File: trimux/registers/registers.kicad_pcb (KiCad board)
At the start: 2 copper layers, 69 parts, among them P1 CONN_02X05, P2 CONN_02X08, P3 CONN_01X04, P4 CONN_01X02, P5 CONN_01X02, P6 CONN_01X02, P7 CONN_01X02, P8 CONN_01X02, P9 CONN_01X02, U1 trimux, U10 trimux, U12 trimux, U2 trimux, U3 trimux, U4 trimux, U5 trimux, U6 trimux, U7 LM324, U8 trimux, U9 trimux

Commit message: registers
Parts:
- added C1: 47u, Capacitors_THT:CP_Radial_D5.0mm_P2.50mm, F.Cu at (91.1, 57.1)
- added C10: 47u, Capacitors_THT:CP_Radial_D5.0mm_P2.50mm, F.Cu at (77.3, 109.2)
- added C11: 47u, Capacitors_THT:CP_Radial_D5.0mm_P2.50mm, F.Cu at (95.1, 106.7)
- added C12: 104, Capacitors_SMD:C_1206_HandSoldering, B.Cu at (66.5, 22.2)
- added C13: 104, Capacitors_SMD:C_1206_HandSoldering, B.Cu at (88.7, 26.0)
- added C14: 104, Capacitors_SMD:C_1206_HandSoldering, B.Cu at (105.2, 24.1)
- added C2: 47u, Capacitors_THT:CP_Radial_D5.0mm_P2.50mm, F.Cu at (74.1, 57.1)
- added C3: 104, Capacitors_SMD:C_1206_HandSoldering, B.Cu at (99.5, 51.4)
- added C4: 104, Capacitors_SMD:C_1206_HandSoldering, B.Cu at (97.0, 47.6)
- added C5: 104, Capacitors_SMD:C_1206_HandSoldering, B.Cu at (75.4, 24.1)
- added C6: 104, Capacitors_SMD:C_1206_HandSoldering, B.Cu at (91.3, 26.0)
- added C7: 104, Capacitors_SMD:C_1206_HandSoldering, B.Cu at (108.4, 24.1)
- added C8: 104, Capacitors_SMD:C_1206_HandSoldering, B.Cu at (84.9, 108.6)
- added C9: 104, Capacitors_SMD:C_1206_HandSoldering, B.Cu at (87.5, 105.4)
- added D1: LED_bicolor, LEDs:LED_D5.0mm, F.Cu at (98.3, 59.1)
- added D2: LED_bicolor, LEDs:LED_D5.0mm, F.Cu at (105.2, 59.1)
- added D3: LED_bicolor, LEDs:LED_D5.0mm, F.Cu at (112.2, 59.1)
- added NPTH1: 1pin, Connectors:1pin, F.Cu at (90.0, 19.2)
- added NPTH2: 1pin, Connectors:1pin, F.Cu at (68.4, 66.7)
- added NPTH3: 1pin, Connectors:1pin, F.Cu at (111.6, 66.7)
- added NPTH4: 1pin, Connectors:1pin, F.Cu at (68.4, 73.0)
- added NPTH5: 1pin, Connectors:1pin, F.Cu at (111.6, 73.0)
- added NPTH6: 1pin, Connectors:1pin, F.Cu at (111.6, 111.8)
- added NPTH7: 1pin, Connectors:1pin, F.Cu at (68.4, 111.8)
- added P1: CONN_02X05, registers:IDC10, F.Cu at (81.8, 64.8)
- added P2: CONN_02X08, registers:IDC16, F.Cu at (109.7, 91.4)
- added P3: CONN_01X04, Pin_Headers:Pin_Header_Straight_1x04_Pitch2.54mm, F.Cu at (67.8, 87.6)
- added P4: CONN_01X02, Pin_Headers:Pin_Header_Straight_1x02_Pitch1.27mm, F.Cu at (73.0, 28.7)
- added P5: CONN_01X02, Pin_Headers:Pin_Header_Straight_1x02_Pitch1.27mm, F.Cu at (80.1, 45.3)
- added P6: CONN_01X02, Pin_Headers:Pin_Header_Straight_1x02_Pitch1.27mm, F.Cu at (82.5, 23.0)
- added P7: CONN_01X02, Pin_Headers:Pin_Header_Straight_1x02_Pitch1.27mm, F.Cu at (99.3, 42.7)
- added P8: CONN_01X02, Pin_Headers:Pin_Header_Straight_1x02_Pitch1.27mm, F.Cu at (97.2, 26.0)
- added P9: CONN_01X02, Pin_Headers:Pin_Header_Straight_1x02_Pitch1.27mm, F.Cu at (113.5, 29.0)
- added R1: 150, Resistors_SMD:R_1206_HandSoldering, B.Cu at (71.6, 33.0)
- added R10: 150, Resistors_SMD:R_1206_HandSoldering, B.Cu at (88.1, 47.6)
- added R11: 150, Resistors_SMD:R_1206_HandSoldering, B.Cu at (91.9, 33.0)
- added R12: 150, Resistors_SMD:R_1206_HandSoldering, B.Cu at (91.9, 40.0)
- added R13: 150, Resistors_SMD:R_1206_HandSoldering, B.Cu at (91.9, 47.6)
- added R14: 330, Resistors_SMD:R_1206_HandSoldering, B.Cu at (107.2, 64.8)
- added R15: 150, Resistors_SMD:R_1206_HandSoldering, B.Cu at (104.6, 33.0)
- added R16: 150, Resistors_SMD:R_1206_HandSoldering, B.Cu at (104.6, 40.0)
- added R17: 150, Resistors_SMD:R_1206_HandSoldering, B.Cu at (104.6, 47.6)
- added R18: 150, Resistors_SMD:R_1206_HandSoldering, B.Cu at (108.4, 33.0)
- added R19: 150, Resistors_SMD:R_1206_HandSoldering, B.Cu at (108.4, 40.0)
- added R2: 150, Resistors_SMD:R_1206_HandSoldering, B.Cu at (71.6, 40.0)
- added R20: 150, Resistors_SMD:R_1206_HandSoldering, B.Cu at (108.4, 47.6)
- added R21: 330, Resistors_SMD:R_1206_HandSoldering, B.Cu at (106.5, 55.2)
- added R22: 330, Resistors_SMD:R_1206_HandSoldering, B.Cu at (113.5, 52.1)
- added R23: 150, Resistors_SMD:R_1206_HandSoldering, B.Cu at (75.9, 90.8)
- added R24: 150, Resistors_SMD:R_1206_HandSoldering, B.Cu at (78.6, 97.7)
- added R25: 150, Resistors_SMD:R_1206_HandSoldering, B.Cu at (75.9, 100.3)
- added R3: 150, Resistors_SMD:R_1206_HandSoldering, B.Cu at (71.6, 47.6)
- added R4: 150, Resistors_SMD:R_1206_HandSoldering, B.Cu at (75.4, 33.0)
- added R5: 150, Resistors_SMD:R_1206_HandSoldering, B.Cu at (75.4, 40.0)
- added R6: 150, Resistors_SMD:R_1206_HandSoldering, B.Cu at (75.4, 47.6)
- added R7: 10k, Resistors_SMD:R_1206_HandSoldering, B.Cu at (71.6, 24.1)
- added R8: 150, Resistors_SMD:R_1206_HandSoldering, B.Cu at (88.1, 33.0)
- added R9: 150, Resistors_SMD:R_1206_HandSoldering, B.Cu at (88.1, 40.0)
- added U1: trimux, trimux:trimux1x15_2.54, F.Cu at (69.0, 17.1)
- added U10: trimux, trimux:trimux1x15_2.54, F.Cu at (81.8, 73.7)
- added U12: trimux, trimux:trimux1x15_2.54, F.Cu at (72.9, 73.7)
- added U2: trimux, trimux:trimux1x15_2.54, F.Cu at (77.9, 17.1)
- added U3: trimux, trimux:trimux1x15_2.54, F.Cu at (85.6, 17.1)
- added U4: trimux, trimux:trimux1x15_2.54, F.Cu at (94.5, 17.1)
- added U5: trimux, trimux:trimux1x15_2.54, F.Cu at (102.1, 17.1)
- added U6: trimux, trimux:trimux1x15_2.54, F.Cu at (111.0, 17.1)
- added U7: LM324, SMD_Packages:SOIC-14_N, B.Cu at (98.9, 65.4)
- added U8: trimux, trimux:trimux1x15_2.54, F.Cu at (99.5, 73.7)
- added U9: trimux, trimux:trimux1x15_2.54, F.Cu at (90.6, 73.7)
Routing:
- net GNDREF: track 276.5 -> 552.9 mm, vias 2 -> 4
- net -5V: track 228.6 -> 457.1 mm, vias 1 -> 2
- net +5V: track 150.8 -> 301.5 mm
- net /CLK: track 97.8 -> 195.7 mm
- net /Qlo: track 93.5 -> 187.1 mm, vias 1 -> 2
- net /Qmi: track 78.8 -> 157.5 mm, vias 1 -> 2
- net /Qhi: track 71.9 -> 143.9 mm, vias 1 -> 2
- net /LO: track 71.6 -> 143.3 mm
- net /Alo: track 60.5 -> 121.0 mm
- net Net-(P2-Pad10): track 54.3 -> 108.7 mm
- net Net-(P2-Pad6): track 52.7 -> 105.3 mm
- net /Ahi: track 51.4 -> 102.7 mm
- net Net-(P2-Pad12): track 48.5 -> 97.0 mm, vias 1 -> 2
- net /Ami: track 44.7 -> 89.4 mm, vias 1 -> 2
- net Net-(C14-Pad1): track 42.2 -> 84.4 mm
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
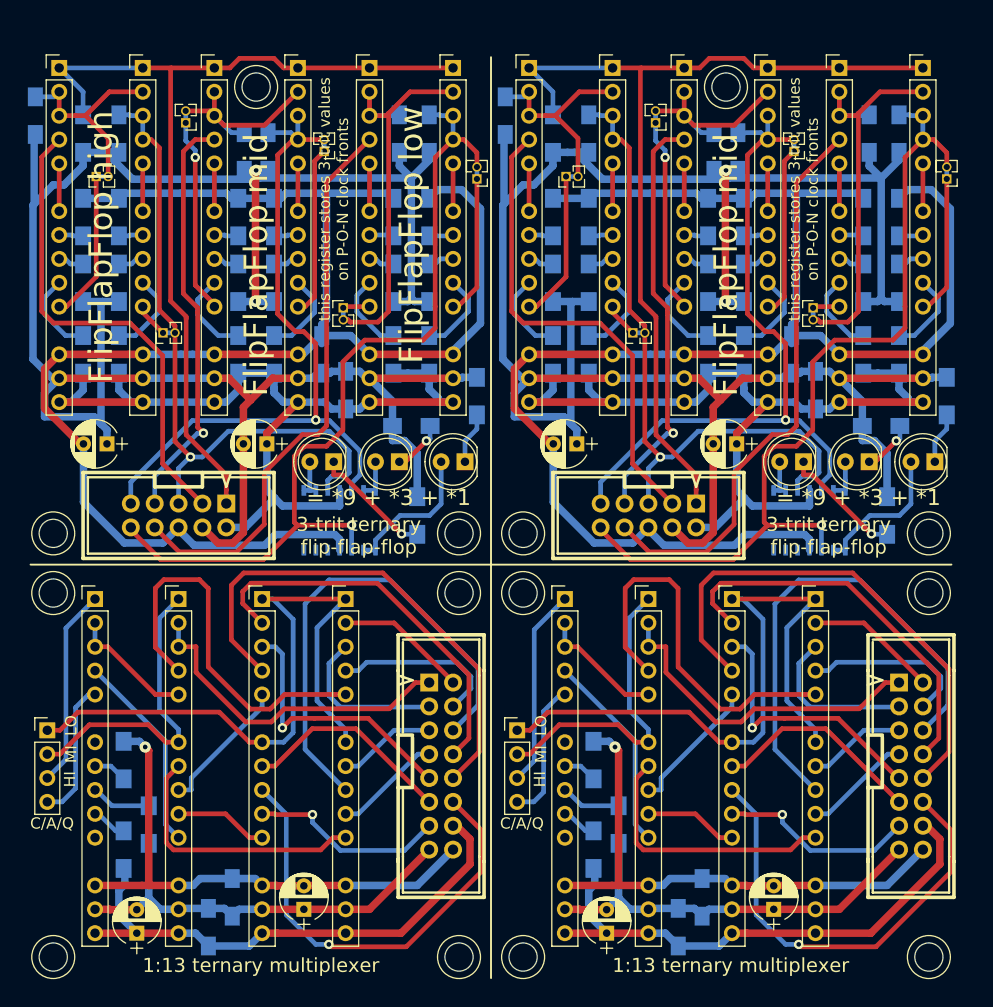
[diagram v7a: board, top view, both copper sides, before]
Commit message: registers bugfix
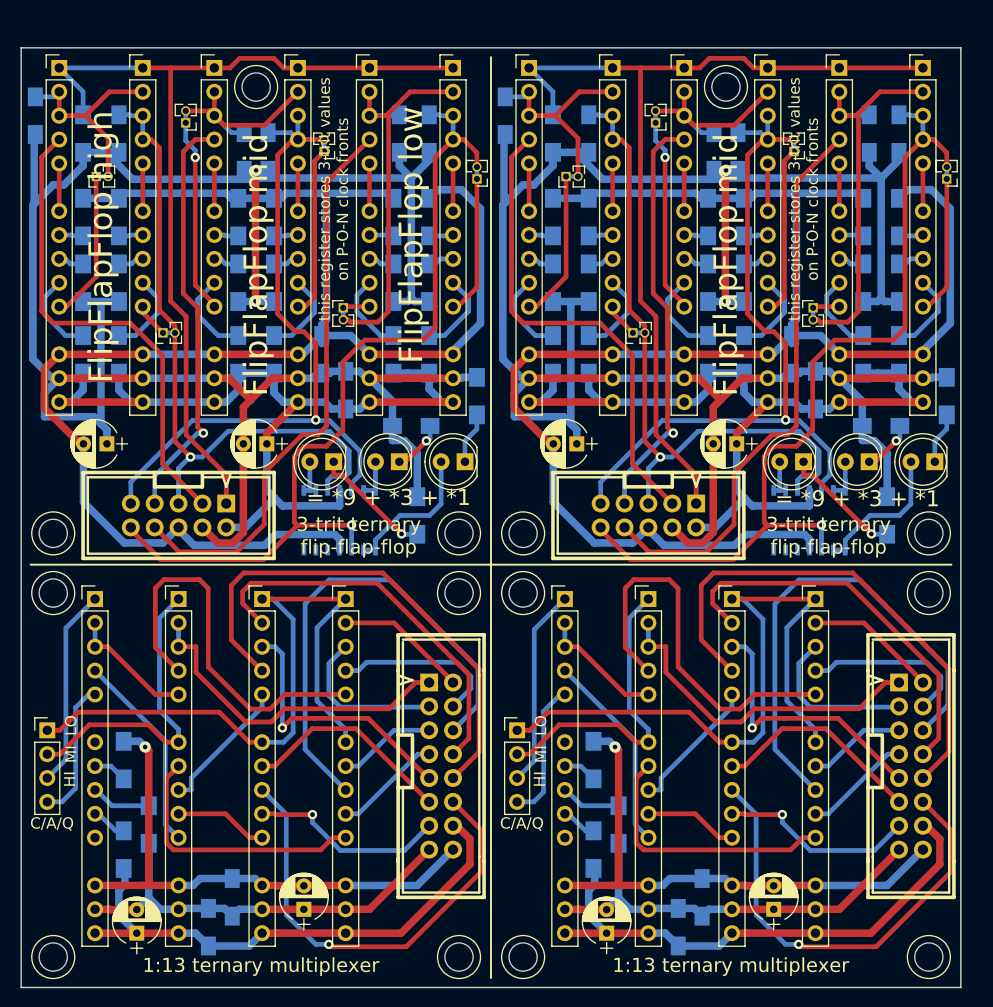
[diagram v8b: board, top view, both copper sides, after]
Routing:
- net Net-(U12-Pad5): track 24.3 -> 26.4 mm
- net /C/A/Q: track 5.39 -> 3.34 mm
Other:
- board outline added: 100 x 100 mm
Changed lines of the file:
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@@
     (links 458)
     (no_connects 86)
-    (area 14.7 14.899999 118.633334 115.935)
+    (area 14.7 14.899999 115.375001 115.100001)
     (thickness 1.6)
-    (drawings 81)
+    (drawings 85)
     (tracks 1354)
     (zones 0)
@@
   (page A4)
   (layers
-    (0 F.Cu signal)
-    (31 B.Cu signal)
+    (0 F.Cu signal hide)
+    (31 B.Cu signal hide)
     (32 B.Adhes user)
     (33 F.Adhes user)
@@
     (41 Cmts.User user)
     (42 Eco1.User user)
-    (43 Eco2.User user)
+    (43 Eco2.User user hide)
     (44 Edge.Cuts user)
     (45 Margin user)
@@
       (effects (font (size 1 1) (thickness 0.15)))
     )
-    (fp_text value CONN_01X02 (at 0 2.965 180) (layer F.Fab) hide
+    (fp_text value CONN_01X02 (at 5.55 3.556 180) (layer F.Fab) hide
       (effects (font (size 1 1) (thickness 0.15)))
     )
@@
       (effects (font (thickness 0.3048)))
     )
-    (fp_text value CONN_02X08 (at 0.254 11.43) (layer F.SilkS) hide
+    (fp_text value CONN_02X08 (at -4.28 11.43) (layer F.SilkS) hide
       (effects (font (thickness 0.3048)))
     )
@@
       (effects (font (size 1 1) (thickness 0.15)))
     )
-    (fp_text value LED_bicolor (at 1.27 3.96 180) (layer F.Fab)
+    (fp_text value LED_bicolor (at 3.01 3.175 180) (layer F.Fab)
       (effects (font (size 1 1) (thickness 0.15)))
     )
@@
       (effects (font (size 1 1) (thickness 0.15)))
     )
-    (fp_text value 1pin (at 0 3) (layer F.Fab) hide
+    (fp_text value 1pin (at 0.165 0) (layer F.Fab) hide
       (effects (font (size 1 1) (thickness 0.15)))
     )
@@
       (effects (font (size 1 1) (thickness 0.15)))
     )
-    (fp_text value 1pin (at 0 3) (layer F.Fab) hide
+    (fp_text value 1pin (at 0.165 0) (layer F.Fab) hide
       (effects (font (size 1 1) (thickness 0.15)))
     )
@@
       (effects (font (size 1 1) (thickness 0.15)))
     )
-    (fp_text value 1pin (at 0 3) (layer F.Fab) hide
+    (fp_text value 1pin (at 0.635 0) (layer F.Fab) hide
       (effects (font (size 1 1) (thickness 0.15)))
     )
@@
       (effects (font (size 1 1) (thickness 0.15)))
     )
-    (fp_text value 1pin (at 0 3) (layer F.Fab) hide
+    (fp_text value 1pin (at 0.635 1.27) (layer F.Fab) hide
       (effects (font (size 1 1) (thickness 0.15)))
     )
@@
     )
   )
+  (gr_line (start 15 15) (end 115 15) (angle 90) (layer Edge.Cuts) (width 0.15))
+  (gr_line (start 15 115) (end 15 15) (angle 90) (layer Edge.Cuts) (width 0.15))
+  (gr_line (start 115 115) (end 15 115) (angle 90) (layer Edge.Cuts) (width 0.15))
+  (gr_line (start 115 15) (end 115 115) (angle 90) (layer Edge.Cuts) (width 0.15))
   (gr_line (start 15 115) (end 115 115) (angle 90) (layer Eco2.User) (width 0.2))
   (gr_text "FlipFlapFlop mid" (at 90.005 38.1 90) (layer F.SilkS)
@@
     (effects (font (size 1.2 1.2) (thickness 0.3)) (justify mirror))
   )
-  (gr_text v26.09.2017 (at 113.754 21.336 90) (layer B.SilkS)
+  (gr_text v26.09.2017 (at 113.5 21.5 90) (layer B.SilkS)
     (effects (font (size 1.2 1.2) (thickness 0.3)) (justify mirror))
   )
@@
     (effects (font (size 1.2 1.2) (thickness 0.3)) (justify mirror))
   )
-  (gr_text "= *9 + *3 + *1" (at 104.102 62.865) (layer F.SilkS)
+  (gr_text "= *9 + *3 + *1" (at 104 63) (layer F.SilkS)
     (effects (font (size 1.7 1.7) (thickness 0.25)))
   )
@@
   (segment (start 22.18 83.82) (end 20.8 85.2) (width 0.5) (layer B.Cu) (net 66))
   (segment (start 20.8 85.2) (end 20.8 93.8) (width 0.5) (layer B.Cu) (net 66))
+  (segment (start 20.8 93.8) (end 19.35 95.25) (width 0.5) (layer B.Cu) (net 66))
   (segment (start 69.55 95.25) (end 67.78 95.25) (width 0.5) (layer B.Cu) (net 67))
   (segment (start 19.35 95.25) (end 17.78 95.25) (width 0.5) (layer B.Cu) (net 67))
-  (segment (start 20.8 93.8) (end 19.35 95.25) (width 0.5) (layer B.Cu) (net 67))
   (segment (start 69.05 22.225) (end 70.781 22.225) (width 0.5) (layer F.Cu) (net 68))
   (segment (start 71.844 22.225) (end 74.384 19.685) (width 0.5) (layer F.Cu) (net 68))
